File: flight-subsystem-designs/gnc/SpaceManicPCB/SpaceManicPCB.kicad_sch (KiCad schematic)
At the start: 12 parts

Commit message: Final Changes
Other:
- sheet GPS Celeste Connector ports: added none; removed I2C1_SCL, I2C1_SDA
- sheet Murgas_Radio_Connector ports: added none; removed I2C1_SCL, I2C1_SDA
- sheet PC104 ports: added none; removed I2C1_SCL, I2C1_SDA

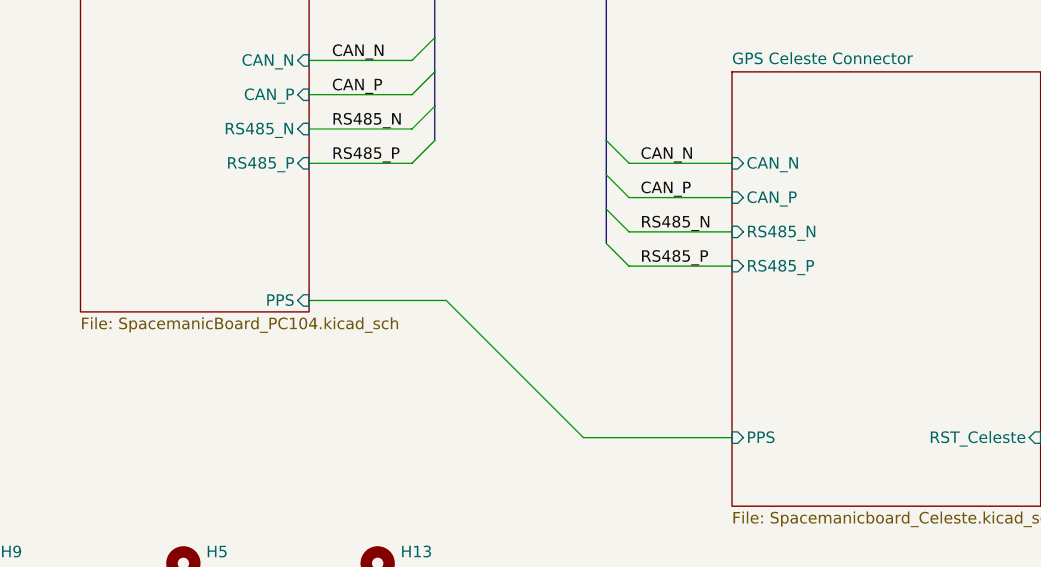
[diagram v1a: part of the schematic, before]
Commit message: Added UART
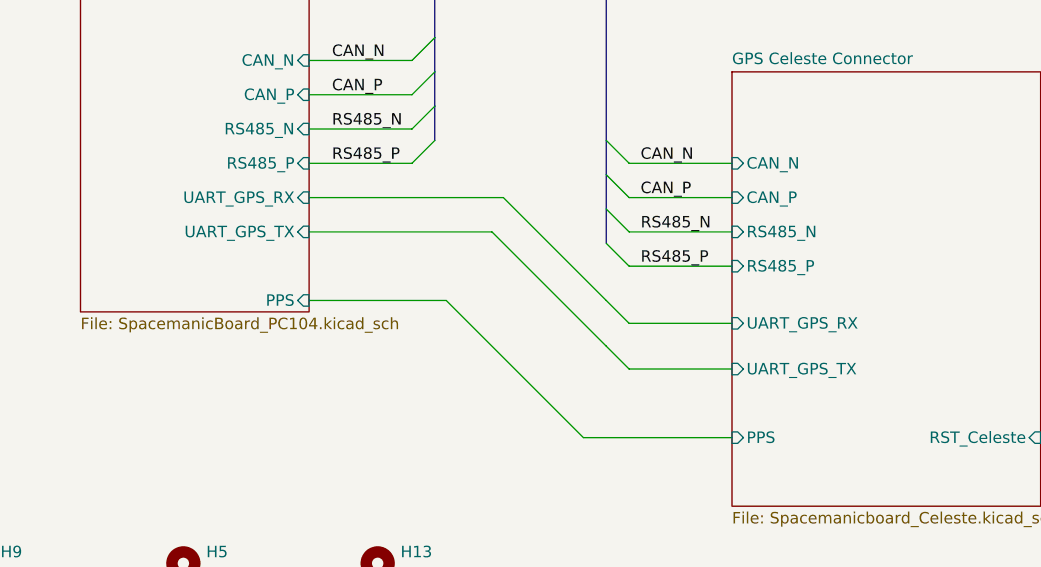
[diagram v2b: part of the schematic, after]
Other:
- sheet GPS Celeste Connector ports: added UART_GPS_RX, UART_GPS_TX; removed none
- sheet PC104 ports: added UART_GPS_RX, UART_GPS_TX; removed none
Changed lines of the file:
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@@
 	)
 	(bus_entry
+		(at 93.98 139.7)
+		(size -2.54 -2.54)
+		(stroke
+			(width 0)
+			(type default)
+		)
+	)
+	(bus_entry
 		(at 69.85 105.41)
 		(size 2.54 -2.54)
@@
 	)
 	(bus_entry
+		(at 93.98 134.62)
+		(size -2.54 -2.54)
+		(stroke
+			(width 0)
+			(type default)
+		)
+	)
+	(bus_entry
 		(at 69.85 116.84)
 		(size 2.54 -2.54)
@@
 		)
 	)
+	(wire
+		(pts
+			(xy 58.42 124.46) (xy 78.74 124.46)
+		)
+		(stroke
+			(width 0)
+			(type default)
+		)
+	)
 	(bus
 		(pts
@@
 	(wire
 		(pts
+			(xy 58.42 120.65) (xy 80.01 120.65)
+		)
+		(stroke
+			(width 0)
+			(type default)
+		)
+	)
+	(wire
+		(pts
+			(xy 80.01 120.65) (xy 91.44 132.08)
+		)
+		(stroke
+			(width 0)
+			(type default)
+		)
+	)
+	(wire
+		(pts
 			(xy 93.98 82.55) (xy 105.41 82.55)
 		)
@@
 	(wire
 		(pts
+			(xy 78.74 124.46) (xy 91.44 137.16)
+		)
+		(stroke
+			(width 0)
+			(type default)
+		)
+	)
+	(wire
+		(pts
 			(xy 93.98 120.65) (xy 105.41 120.65)
 		)
@@
 	(wire
 		(pts
+			(xy 93.98 134.62) (xy 105.41 134.62)
+		)
+		(stroke
+			(width 0)
+			(type default)
+		)
+	)
+	(wire
+		(pts
 			(xy 39.37 165.1) (xy 39.37 172.72)
 		)
@@
 		)
 	)
+	(wire
+		(pts
+			(xy 93.98 139.7) (xy 105.41 139.7)
+		)
+		(stroke
+			(width 0)
+			(type default)
+		)
+	)
 	(bus
 		(pts
@@
 			)
 		)
+		(pin "UART_GPS_RX" input
+			(at 58.42 120.65 0)
+			(effects
+				(font
+					(size 1.27 1.27)
+				)
+				(justify right)
+			)
+		)
+		(pin "UART_GPS_TX" input
+			(at 58.42 124.46 0)
+			(effects
+				(font
+					(size 1.27 1.27)
+				)
+				(justify right)
+			)
+		)
 		(instances
 			(project "SpaceManicPCB"
@@
 			(effects
 				(font
+					(size 1.27 1.27)
+				)
+				(justify left)
+			)
+		)
+		(pin "UART_GPS_RX" input
+			(at 105.41 134.62 180)
+			(effects
+				(font
+					(size 1.27 1.27)
+				)
+				(justify left)
+			)
+		)
+		(pin "UART_GPS_TX" input
+			(at 105.41 139.7 180)
+			(effects
+				(font
